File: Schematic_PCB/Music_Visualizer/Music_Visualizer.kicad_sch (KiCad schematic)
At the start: 116 parts, among them U2 LM324, U3 LM324, U4 LM324, U5 LM324, U6 LM324

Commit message: Added audio signal circuitry
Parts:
- removed V1, V2: (no value), symbol Device:Battery_Cell
- removed V3: (no value), symbol pspice:VSOURCE
- added J1: (no value), symbol Connector:AudioJack2_Ground
- added JP1: (no value), symbol Jumper:SolderJumper_2_Open
- added SW1: (no value), symbol Switch:SW_SPDT
- U1: value (none) -> LM324; footprint (none) -> Package_SO:SOIC-14_3.9x8.7mm_P1.27mm
- U6: value LM324 -> (none)
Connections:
- net GND: now also J1.S, JP1.1 (A)
- net Vsig: now also SW1.2 (B)
- new net: J1.T, SW1.3 (C)
- new net Vsig_male: JP1.2 (B), SW1.1 (A)
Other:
- note added: "Audio Signal Input"
- note added: "Op-Amp Power (+/-5V)"
- moved on the sheet: C19, C20, C21, C22, C23, C24, R29, R30, R31, R32, R33, R34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

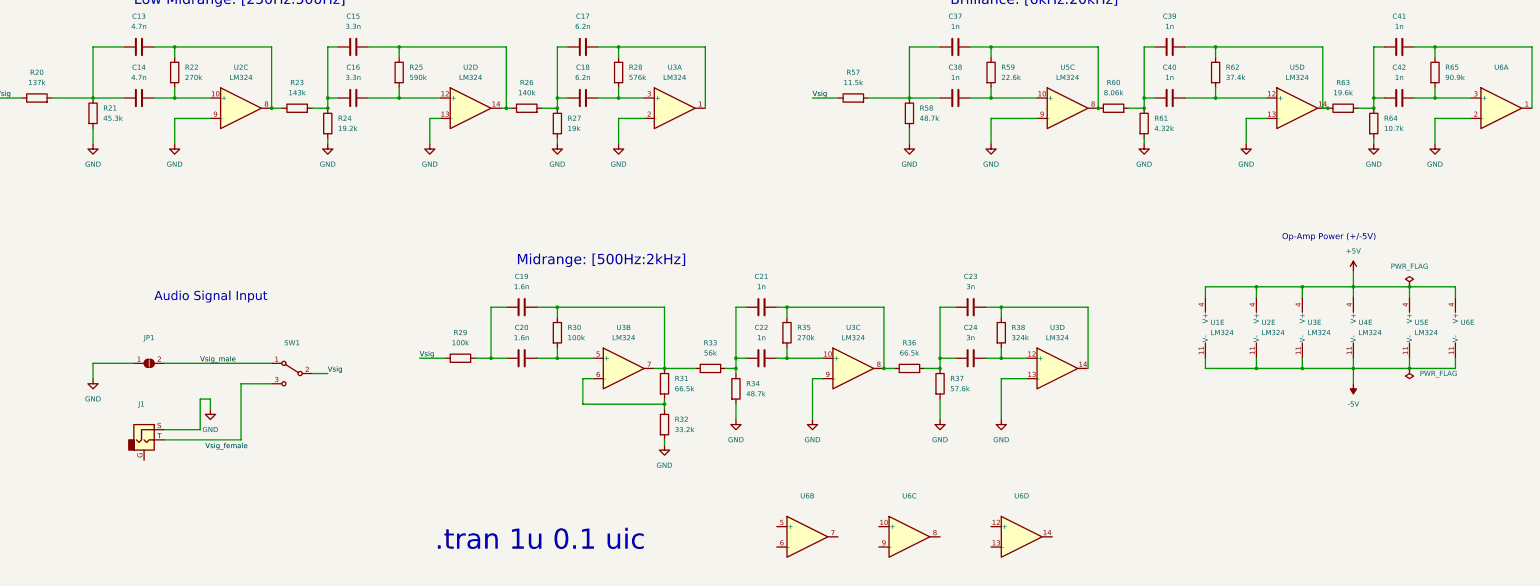
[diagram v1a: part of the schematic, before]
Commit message: Finished power circuitry schematic and updated BOM
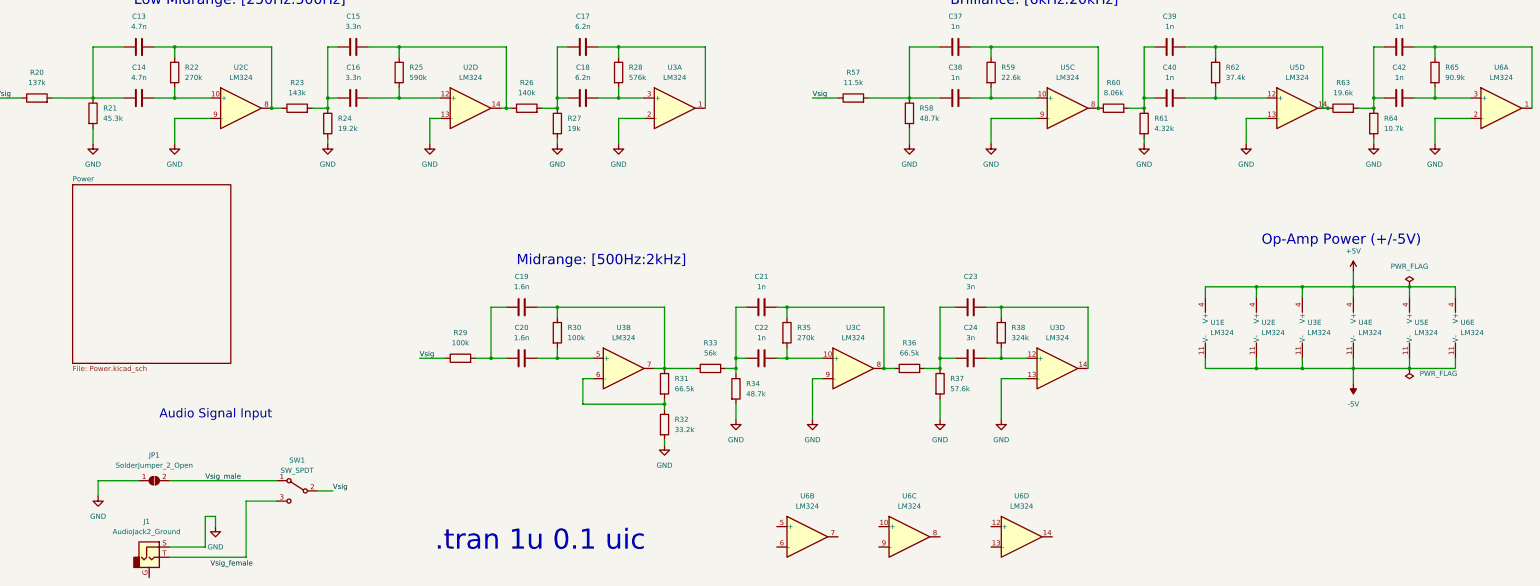
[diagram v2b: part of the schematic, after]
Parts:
- J1: value (none) -> AudioJack2_Ground; footprint (none) -> Connector_Audio:Jack_3.5mm_CUI_SJ-3523-SMT_Horizontal
- JP1: value (none) -> SolderJumper_2_Open; footprint (none) -> Jumper:SolderJumper-2_P1.3mm_Open_Pad1.0x1.5mm
- SW1: value (none) -> SW_SPDT; footprint (none) -> local:SW_OS102011MS2QN1
- U6: value (none) -> LM324; footprint (none) -> Package_SO:SOIC-14_3.9x8.7mm_P1.27mm
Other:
- added sheet Power (Power.kicad_sch)
- moved on the sheet: J1, JP1, SW1

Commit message: Completed and annotated Spectrum filters and power circuitry, and updated BOM
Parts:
- added C43, C45, C47: (no value), symbol Device:C
- added C44: 100u, Capacitor_SMD:C_1206_3216Metric, symbol Device:C
- added C46: 10u, Capacitor_SMD:C_0805_2012Metric, symbol Device:C
- added C48, C49: 1u, Capacitor_SMD:C_0402_1005Metric, symbol Device:C
- added R66, R67, R68, R69, R70, R71, R72: (no value), symbol Device:R
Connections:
- net GND: now also R66.2, R67.2, R68.2, R69.2, R70.2, R71.2, R72.2
- net at C23.2, R38.1, U3.14: now also C46.1
- net at C11.2, R19.1, U2.7: now also C44.1
- net at C41.2, R65.1, U6.1: now also C49.1
- net at C17.2, R28.1, U3.1: now also C45.1
- net at C29.2, R47.1, U4.8: now also C47.1
- net at C5.2, R9.1, U1.8: now also C43.1
- net at C35.2, R56.1, U5.7: now also C48.1
- new net VBass: C44.2, R67.1
- new net VBrilliance: C49.2, R72.1
- new net VLowerMidrange: C45.2, R68.1
- new net VMidrange: C46.2, R69.1
- new net VPresence: C48.2, R71.1
- new net VSubBass: C43.2, R66.1
- new net VUpperMidrange: C47.2, R70.1
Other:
- moved on the sheet: C1, C10, C11, C12, C13, C14, C15, C16, C17, C18, C19, C2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

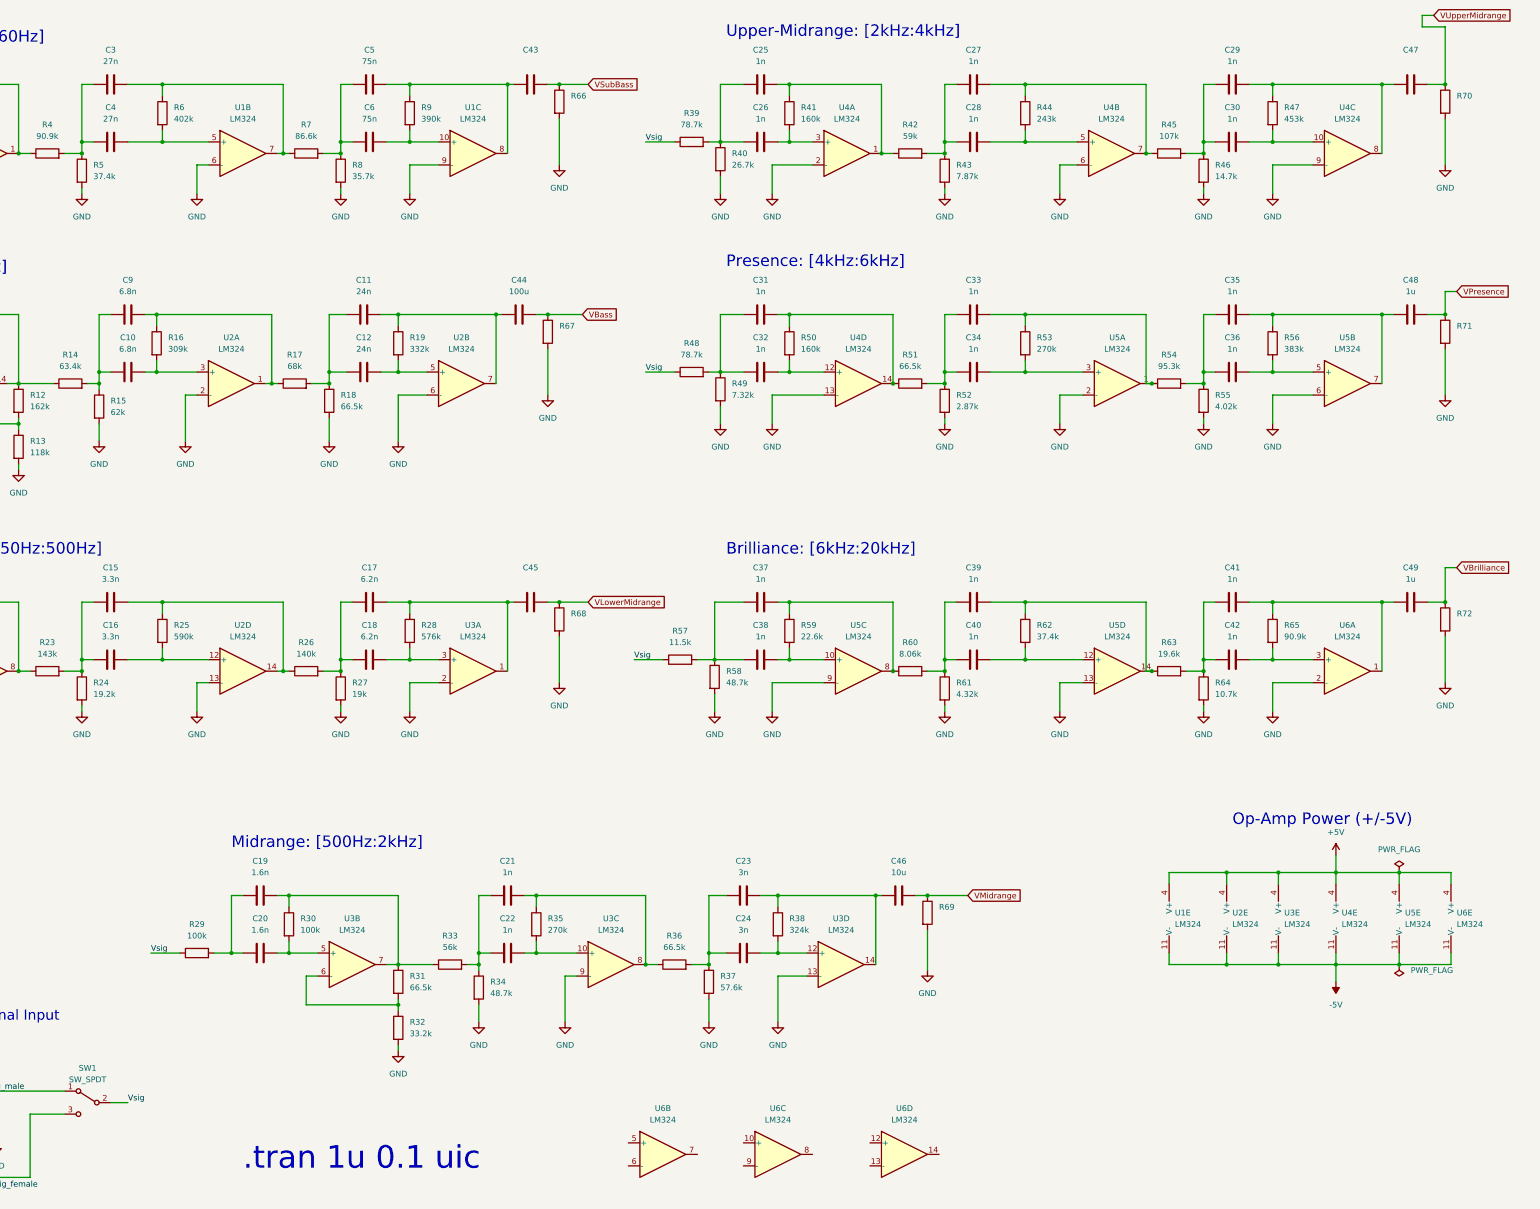
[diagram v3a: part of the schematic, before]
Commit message: Finished LED Driver Sub-Circuit and updated BOM
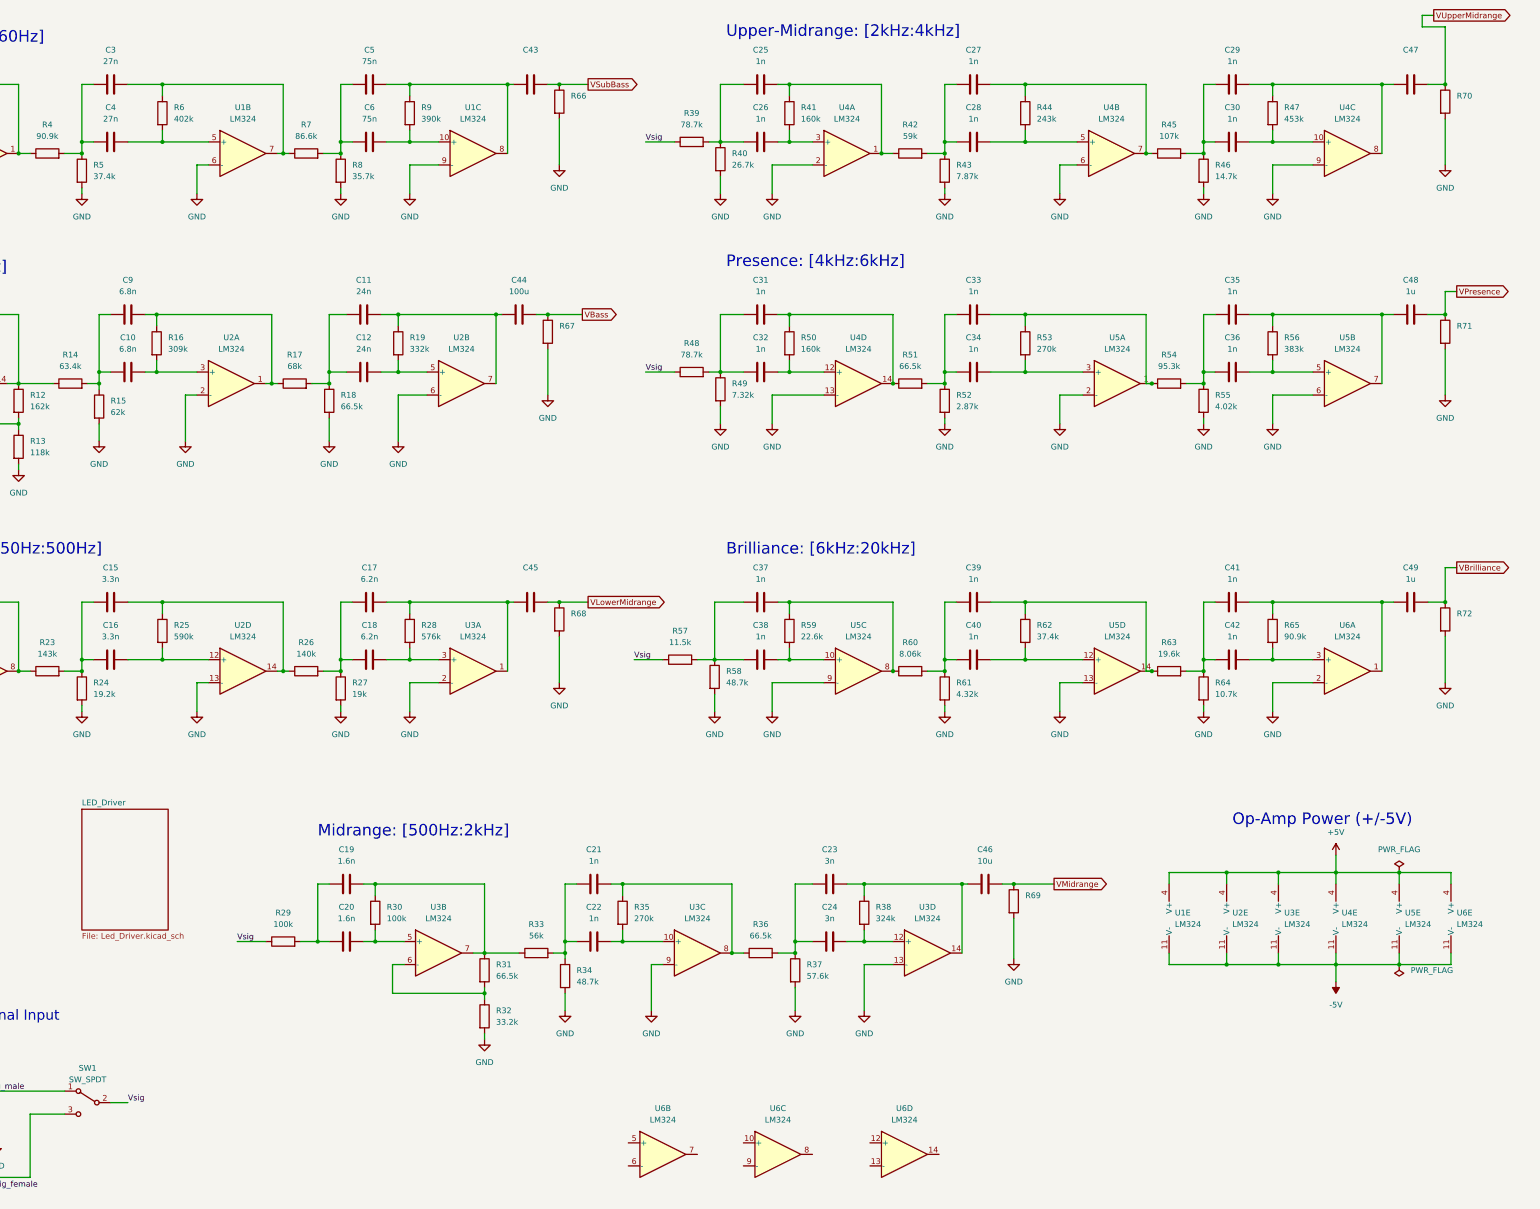
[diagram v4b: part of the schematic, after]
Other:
- added sheet LED_Driver (Led_Driver.kicad_sch)
- note removed: ".tran 1u 0.1 uic"
- moved on the sheet: C19, C20, C21, C22, C23, C24, C46, R29, R30, R31, R32, R33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
